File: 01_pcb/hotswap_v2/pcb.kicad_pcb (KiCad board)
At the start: 2 copper layers, 251.2 x 81.3 mm, 131 parts, among them J1 TYPE-C-31-M12_13, J2 AVR-ISP-6_mod, J3 Conn_01x01, J4 Conn_01x01, J5 Conn_01x01, J6 Conn_01x01, J7 Conn_01x01, K1 KEYSW, K10 KEYSW, K12 KEYSW, K13 KEYSW, K14 KEYSW, K15 KEYSW, K16 KEYSW, K17 KEYSW, K18 KEYSW, K19 KEYSW, K2 KEYSW, K20 KEYSW, K21 KEYSW, K23 KEYSW, K24 KEYSW, K25 KEYSW, K26 KEYSW, K27 KEYSW, K28 KEYSW, K29 KEYSW, K3 KEYSW, K30 KEYSW, K31 KEYSW, K32 KEYSW, K33 KEYSW, K34 KEYSW, K36 KEYSW, K37 KEYSW, K38 KEYSW, K39 KEYSW, K4 KEYSW, K42 KEYSW, K43 KEYSW, K44 KEYSW, K45 KEYSW, K46 KEYSW, K47 KEYSW, K48 KEYSW, K5 KEYSW, K50 KEYSW, K51 KEYSW, K52 KEYSW, K6 KEYSW, K7 KEYSW, K8 KEYSW, K9 KEYSW, SW1 SW_PUSH, SW2 Rotary_Encoder_Switch, U1 ATMEGA32U4, U2 PRTR5V0U2X, Y1 16MHz

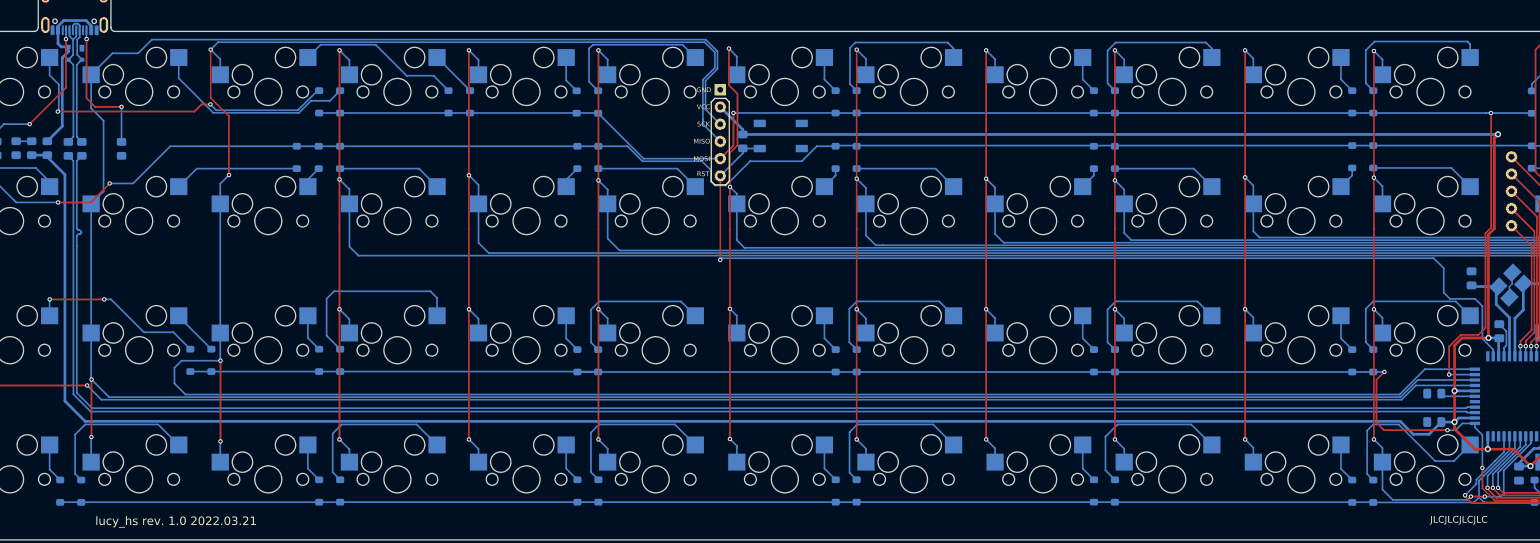
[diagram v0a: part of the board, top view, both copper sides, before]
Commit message: making HS pcb flexy
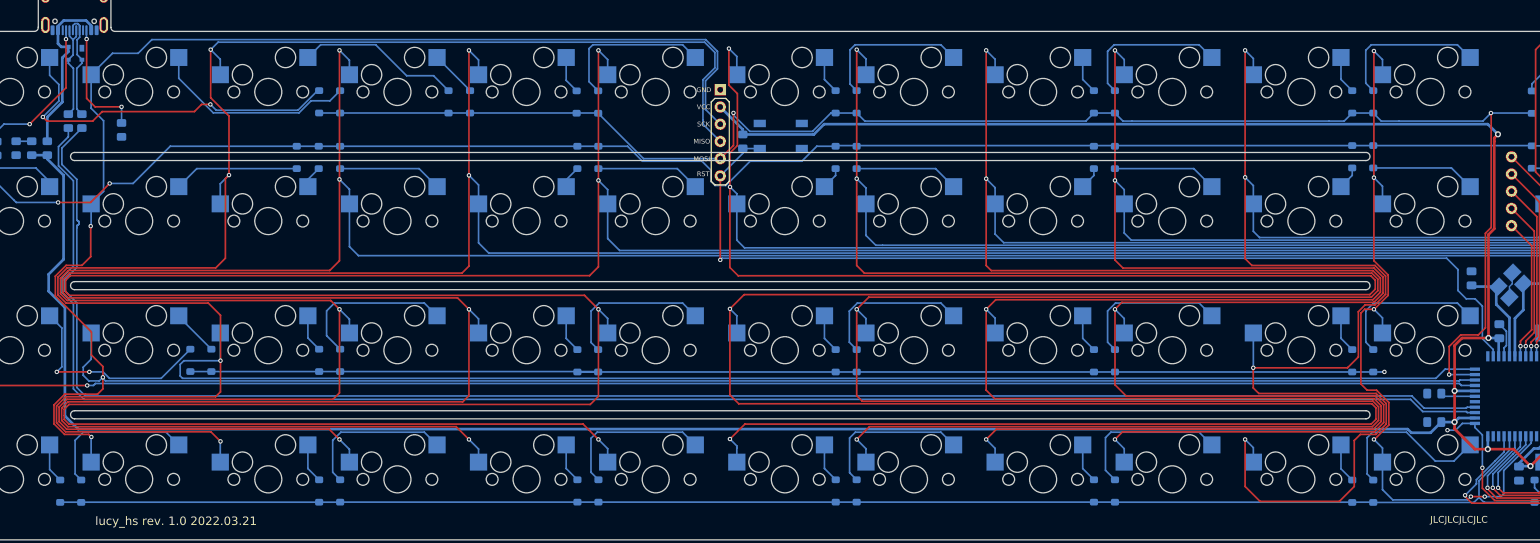
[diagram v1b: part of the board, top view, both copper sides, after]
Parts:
- moved R2 4.10 mm to (95.5, 57.5)
- moved R3 4.10 mm to (97.5, 57.5)
- moved RCC2 2.80 mm to (103.3, 58.8)
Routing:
- net col6: track 241.5 -> 616.9 mm
- net col5: track 252.1 -> 561.4 mm
- net col7: track 223.7 -> 526.1 mm
- net col4: track 271.5 -> 506.1 mm
- net col8: track 206.2 -> 433.6 mm
- net col3: track 289.4 -> 448.8 mm
- net col9: track 188.6 -> 340.9 mm
- net col2: track 360.8 -> 456.2 mm
- net col10: track 171.3 -> 262.1 mm
- net col1: track 372.5 -> 395.9 mm, vias 2 -> 3
- net row2: track 252.9 -> 234.0 mm
- net col11: track 106.7 -> 113.5 mm
- net D+: track 243.3 -> 249.8 mm
- net D-: track 243.4 -> 249.6 mm
- net row0: track 234.0 -> 239.2 mm
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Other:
- outline, holes or cut-outs redrawn

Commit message: backups
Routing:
- net col6: track 616.9 -> 241.5 mm
- net col5: track 561.4 -> 252.1 mm
- net col7: track 526.1 -> 223.7 mm
- net col4: track 506.1 -> 271.5 mm
- net col8: track 433.6 -> 206.2 mm
- net col3: track 448.8 -> 289.4 mm
- net col9: track 340.9 -> 188.6 mm
- net col2: track 456.2 -> 365.6 mm
- net col10: track 262.1 -> 171.7 mm
- net col1: track 395.9 -> 380.7 mm
- net row2: track 234.0 -> 247.2 mm
- net col11: track 113.5 -> 109.1 mm
- net GND: track 9.17 -> 10.7 mm, vias 0 -> 1
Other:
- outline, holes or cut-outs redrawn

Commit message: route lines away from crystal
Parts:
- moved D14 19.5 mm to (113.5, 74.4), turned to 90 degrees
- moved D23 11.6 mm to (284.9, 74.4), turned to 90 degrees
- moved D24 11.6 mm to (288.0, 74.4), turned to 90 degrees
- moved D19 11.5 mm to (208.9, 74.4), turned to 90 degrees
- moved D20 11.5 mm to (212.0, 74.4), turned to 90 degrees
- moved D17 11.5 mm to (170.5, 74.4), turned to 90 degrees
- moved D18 11.5 mm to (173.6, 74.4), turned to 90 degrees
- moved D15 11.5 mm to (132.4, 74.4), turned to 90 degrees
- moved D16 11.5 mm to (135.6, 74.4), turned to 90 degrees
- moved D21 11.5 mm to (246.8, 74.4), turned to 90 degrees
- moved D22 11.5 mm to (249.9, 74.4), turned to 90 degrees
- moved J2 5.43 mm to (191.7, 47.4)
- moved RSW1 1.70 mm to (195.0, 58.8)
- moved D13 0.80 mm to (82.1, 60.8), turned to 90 degrees
- moved SW1 0.40 mm to (200.6, 59.3)
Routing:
- net row1: track 356.7 -> 418.3 mm
- net ISP_Reset: track 145.5 -> 159.5 mm, vias 1 -> 2
- net Net-(D14-Pad2): track 18.5 -> 6.29 mm
- net col12: track 93.7 -> 104.0 mm, vias 7 -> 5
- net col2: track 365.6 -> 355.9 mm
- net Net-(D20-Pad2): track 15.4 -> 23.8 mm
- net Net-(D24-Pad2): track 15.4 -> 23.8 mm
- net Net-(D16-Pad2): track 15.4 -> 23.7 mm
- net Net-(D22-Pad2): track 15.4 -> 23.6 mm
- net Net-(D18-Pad2): track 15.4 -> 23.6 mm
- net VCC: track 470.0 -> 478.0 mm, vias 7 -> 8
- net col10: track 171.7 -> 179.4 mm
- net row0: track 239.2 -> 231.8 mm, vias 3 -> 2
- net col6: track 241.5 -> 234.8 mm
- net Net-(J3-Pad1): track 21.2 -> 26.6 mm
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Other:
- board text added: "lucy_hs_flex rev 1.0"
- board text added: "lucy_hs_flex rev. 1.0 2022.03.21"
- board text removed: "lucy_hs rev 1.0"
- board text removed: "lucy_hs rev. 1.0 2022.03.21"
